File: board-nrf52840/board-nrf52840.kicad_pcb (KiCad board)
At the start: 2 copper layers, 32 x 32 mm, 59 parts, among them J1 USB_OTG, J2 SWD, J3 Alternative_power, J4 Conn_01x05_Female, J5 I2C_sensors, Q1 CMXDM7002A, SW1 SW_SPDT_GND, U1 bq21040, U10 SiP32475, U11 OPT3001, U12 SiP32475, U13 LDK120_, U2 BQ29733DSER, U3 USBLC6-2P6, U4 LPS22HBTR, U6 ICM-20948, U7 HTS221, U8 BMD-340-A-R, U9 AT45DB641E-MHN-Y, Y1 Crystal

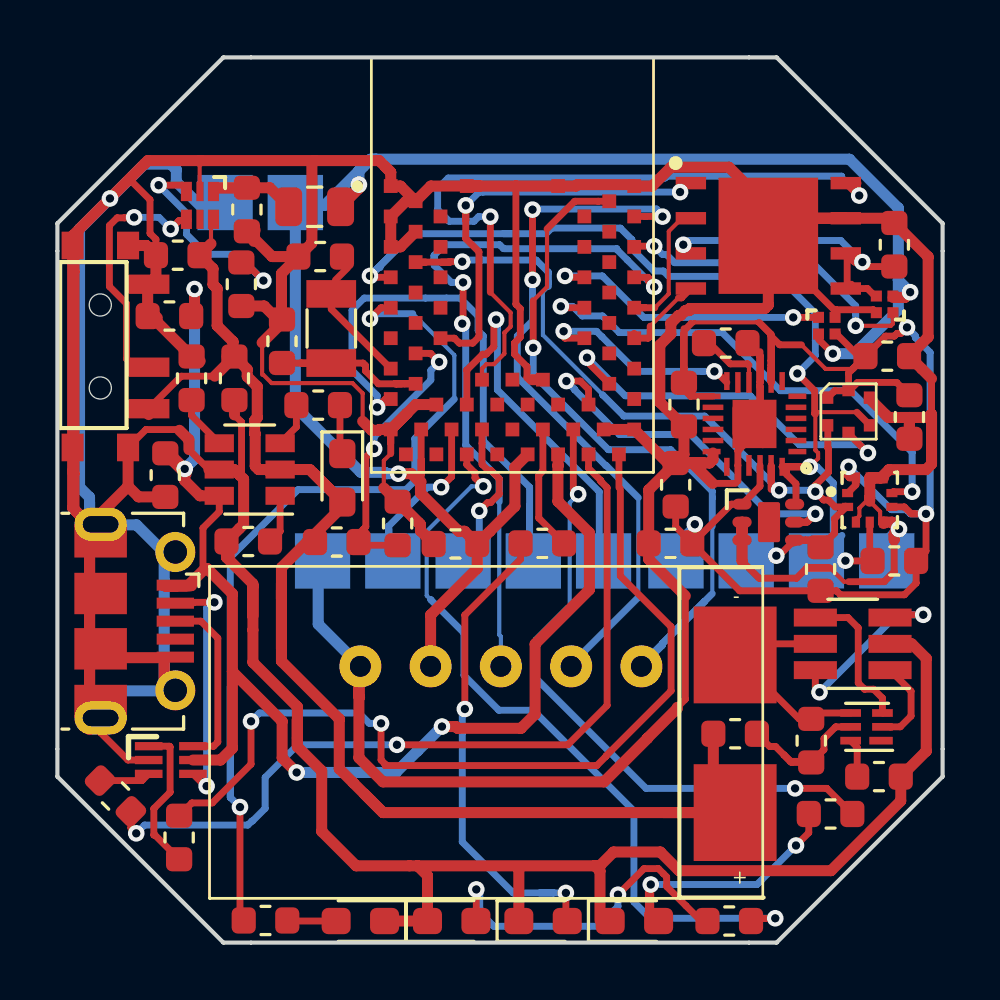
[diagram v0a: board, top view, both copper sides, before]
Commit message: Fixed 3d models and footptints
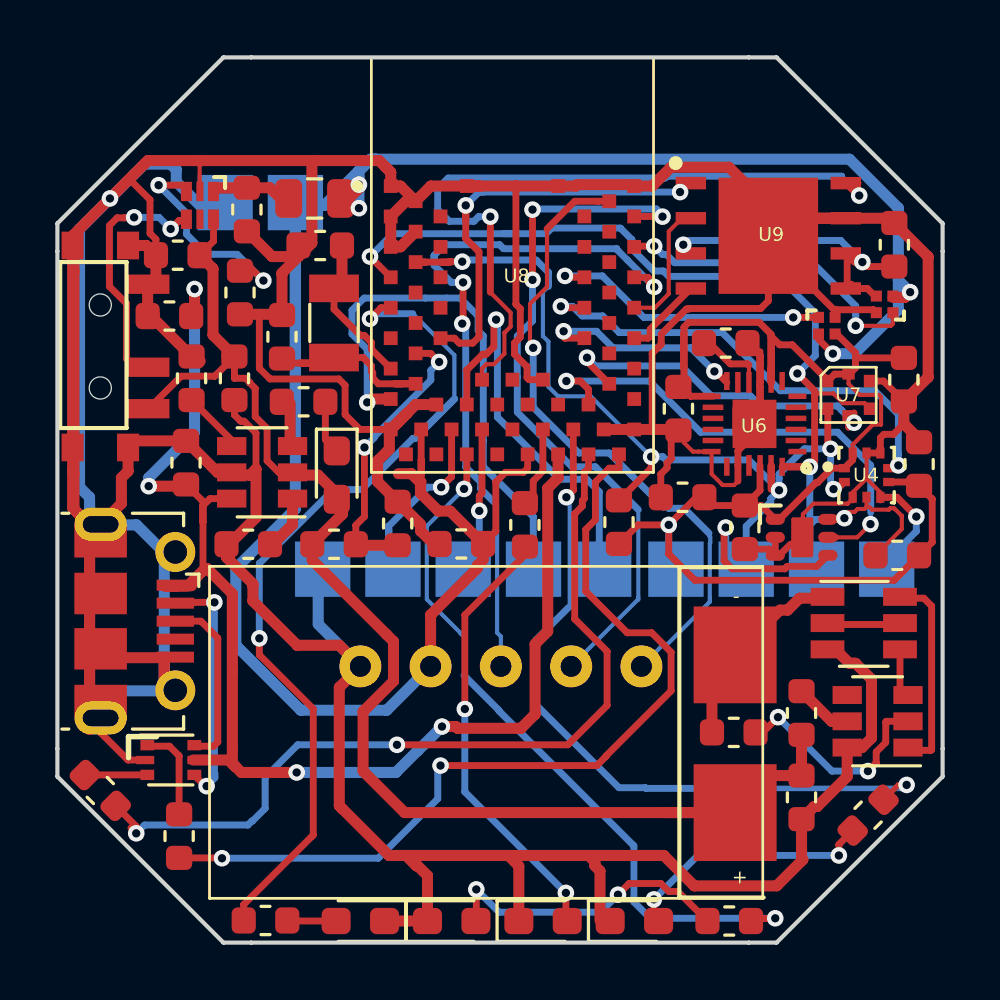
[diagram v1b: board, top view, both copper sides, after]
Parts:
- Q1: value CMXDM7002A -> SMC8205AS; footprint Package_TO_SOT_SMD:SOT-23-6_Handsoldering -> Package_TO_SOT_SMD:TSOT-23-6
- R3: value 330R -> 100R
- R4: value 6k -> 10k
- R5: value 2.2k -> 1k
- SW1: footprint hydra:PCM12SMTR -> ss:PCM12SMTR
- U2: value BQ29733DSER -> DW01; footprint Package_SON:WSON-6_1.5x1.5mm_P0.5mm -> Package_TO_SOT_SMD:SOT-23-6
- U3: footprint hydra:SOT-666 -> Package_TO_SOT_SMD:SOT-666
- U6: value ICM-20948 -> Val**
- U7: footprint hydra:HLGA-6L -> ss:HLGA-6L
- moved C9 8.36 mm to (121.5, 111.7)
- moved C10 8.00 mm to (129.6, 110.7)
- moved R8 7.48 mm to (119.3, 115.8)
- moved R5 5.49 mm to (123.5, 123.4)
- moved C5 4.07 mm to (130.2, 113.7), turned to 270 degrees
- moved C17 2.75 mm to (123.8, 116.0), turned to 90 degrees
- moved R3 2.51 mm to (125.9, 122.7), turned to 270 degrees
- moved C4 2.08 mm to (125.9, 125.8)
- moved R12 1.36 mm to (128.3, 126.4), turned to 45 degrees
- moved U11 1.32 mm to (125.9, 116.5)
- moved R13 0.92 mm to (115.9, 115.9), turned to 90 degrees
- moved U4 0.91 mm to (128.2, 114.1)
- moved C1 0.87 mm to (103.7, 113.7), turned to 90 degrees
- moved Q1 0.85 mm to (128.2, 119.5), turned to 0 degrees
- moved U7 0.60 mm to (127.6, 111.2)
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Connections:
- C4 pad 1: Net-(C4-Pad1) -> GND
- C4 pad 2: Net-(BT1-Pad2) -> V_BAT
- Q1 pad 1: Net-(Q1-Pad1) -> Net-(BT1-Pad2)
- Q1 pad 2: GND -> Net-(Q1-Pad2)
- Q1 pad 3: Net-(Q1-Pad3) -> GND
- Q1 pad 5: Net-(BT1-Pad2) -> Net-(Q1-Pad2)
- Q1 pad 6: Net-(Q1-Pad3) -> Net-(Q1-Pad6)
- R3 pad 1: Net-(C4-Pad1) -> Net-(R3-Pad1)
- R5 pad 1: GND -> Net-(R5-Pad1)
- R5 pad 2: Net-(R5-Pad2) -> Net-(BT1-Pad2)
- U2 pad 1: Net-(U2-Pad1) -> Net-(Q1-Pad6)
- U2 pad 2: Net-(Q1-Pad1) -> Net-(R5-Pad1)
- U2 pad 4: Net-(BT1-Pad2) -> Net-(U2-Pad4)
- U2 pad 5: Net-(C4-Pad1) -> Net-(R3-Pad1)
- U2 pad 6: Net-(R5-Pad2) -> GND
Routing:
- net GND: track 339.0 -> 298.9 mm
- net VCC: track 62.2 -> 85.4 mm
- net I2C_SCL: track 33.2 -> 43.0 mm, vias 4 -> 6
- net Net-(R5-Pad1): track 0.00 -> 7.96 mm, vias 0 -> 2
- net Net-(Q1-Pad6): track 0.00 -> 7.67 mm
- net Net-(Q1-Pad3): track 7.01 -> 0.00 mm, vias 2 -> 0
- net VCCQ: track 61.1 -> 54.7 mm, vias 4 -> 1
- net Net-(C4-Pad1): track 5.60 -> 0.00 mm
- net V_BAT: track 58.4 -> 54.2 mm
- net INT_OPT3004: track 14.0 -> 18.1 mm
- net Net-(Q1-Pad4): track 5.56 -> 1.84 mm
- net Net-(Q1-Pad1): track 3.46 -> 0.00 mm
- net SWDIO: track 27.1 -> 23.6 mm
- net P0.11: track 23.3 -> 26.1 mm
- net Net-(Q1-Pad2): track 0.00 -> 2.62 mm
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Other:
- board text added: "R&D SoftServe 2019 rev. 1.1"
- board text removed: "R&D SoftServe 2019 rev. 1.0"
